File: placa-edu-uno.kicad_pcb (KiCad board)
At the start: 2 copper layers, 96 x 96 mm, 44 parts, among them J1 Conn_02x20_Odd_Even_MountingP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, J10 HEADER, J3 Screw_Terminal_01x02, J4 Screw_Terminal_01x02, J5 Screw_Terminal_01x02, J6 Conn_02x13_Odd_Even, J7 HEADER, J8 HEADER, J9 HEADER, U1 PCA9685, U2 MAX98357A, U3 MAX98357A, U4 ICS-43434, U5 ICS-43434

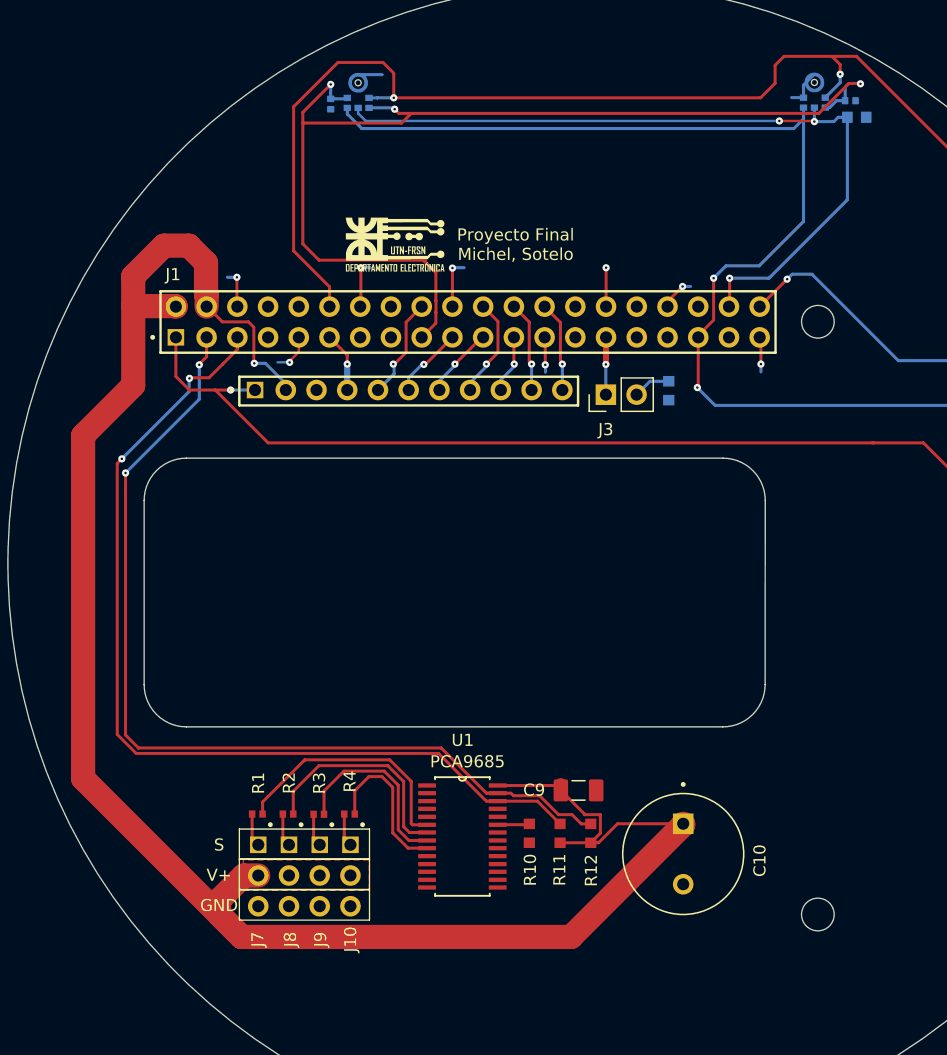
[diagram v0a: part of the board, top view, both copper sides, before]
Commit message: Se centraron los microfonos a 19 mm del centro de la placa
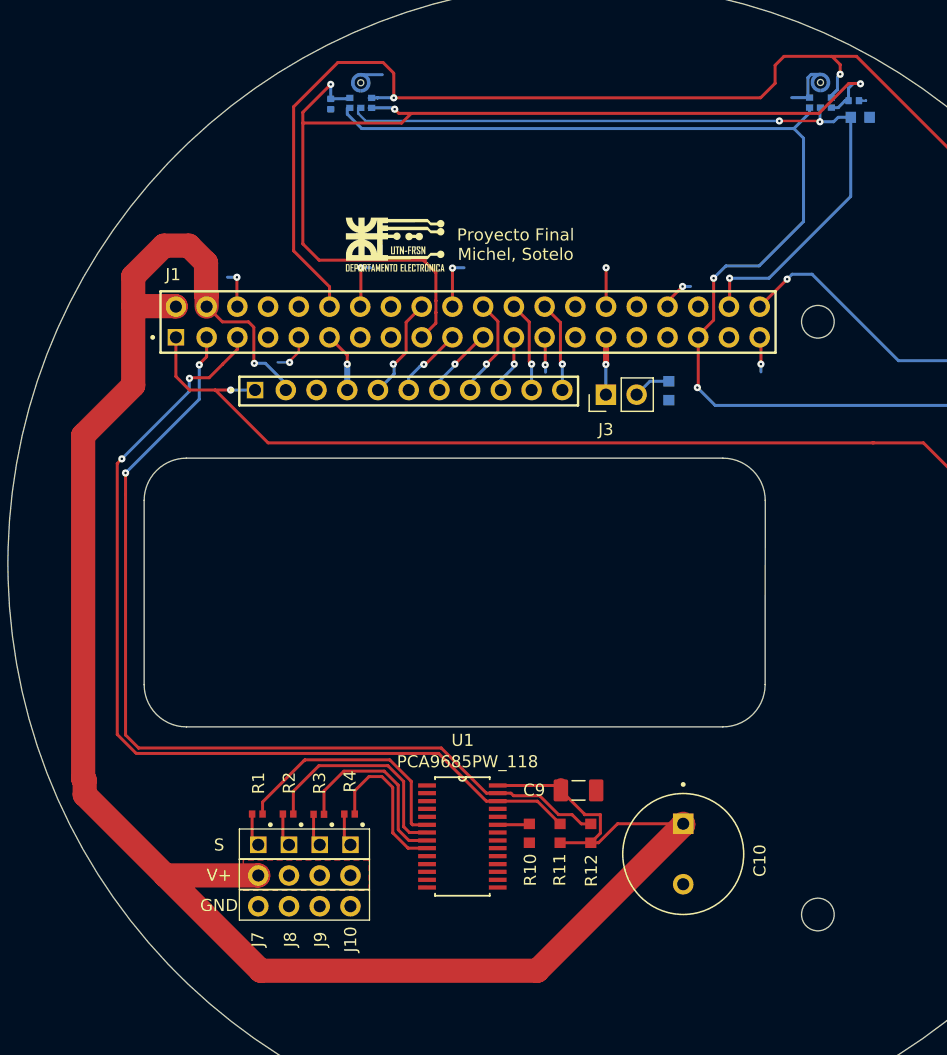
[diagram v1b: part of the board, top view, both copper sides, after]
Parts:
- U1: value PCA9685 -> PCA9685PW_118
- moved U4 0.50 mm to (61.7, -15.6)
- moved R15 0.28 mm to (65.0, -13.4)
- moved C11 0.28 mm to (64.5, -14.8)
- moved U5 0.22 mm to (23.7, -15.5)
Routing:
- net 5V_RPI: track 159.9 -> 162.7 mm
- net GND: track 54.6 -> 56.0 mm
- net GPIO_19_FS_PCM: track 120.3 -> 119.5 mm
